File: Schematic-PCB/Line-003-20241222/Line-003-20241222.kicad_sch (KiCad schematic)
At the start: 233 parts, among them J1 Conn_MD, J2 VIN, SW1 RESET, U47 LM393, U48 LM393, U49 LM393, U50 LM393, U51 LM393, U52 LM393, U53 LM393, U54 LM393, U55 LM393, U56 LM393, U57 LM393, U58 LM393, U59 LM393, U60 LM393, U61 LM393, U62 LM393, U63 LM393, U64 LM393, U65 ATmega2560 Pro Board

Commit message: update: ラインセンサ基板 ver.003 を更新した
回路図のDRをした
いろいろ問題点ありそうだから、明日もう一回DRし直してからPCBいこか
出来れば明日、無理なら明後日ぐらいまでに必ず完成させよう！！
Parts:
- removed C14, C15, C16: 0.1uF, symbol Device:C_Small
- removed U60, U61, U62: LM393, symbol Comparator:LM393
- added JP10, JP7, JP8, JP9: Jumper_2_Small_Open, Jumper:SolderJumper-2_P1.3mm_Open_Pad1.0x1.5mm, symbol Jumper:Jumper_2_Small_Open
- added R86, R87: 100, Resistor_SMD:R_0603_1608Metric, symbol Device:R_Small
- C1, C10, C11, C12, C13, C17, C18, C2, C3, C4, C5, C6, C7, C8, C9: value 0.1uF -> 100nF; footprint (none) -> Capacitor_SMD:C_0603_1608Metric
- C21: renamed from C20; value C_Small -> 100nF; footprint (none) -> Capacitor_SMD:C_0603_1608Metric
- C23: footprint Capacitor_SMD:C_0603_1608Metric -> (none)
- R27, R28, R29, R30: value Line-PDWN -> Line-PDWN2
- U47, U48, U49, U50, U51, U52, U53, U54, U55, U56, U57, U58, U59, U63, U64: footprint (none) -> Package_SO:SOIC-8_3.9x4.9mm_P1.27mm
- renumbered C21 to C20, J2 to J1, J1 to J2, R78 to R77, R79 to R78, R80 to R79, R81 to R80, R82 to R81, R83 to R82, R84 to R83, R85 to R84, R86 to R85, R87 to R88
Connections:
- net 01: no longer U49.1, U50.1, U51.1, U52.1, U53.1, U54.1, U55.1, U56.1, U57.1, U58.1, U59.1
- net 02: no longer U49.7, U50.7, U51.7, U52.7, U53.7, U54.7, U55.7, U56.7, U57.7, U58.7, U59.7
- net 05: now also U49.1
- net 06: now also U49.7
- net 07: now also U50.1
- net 08: now also U50.7
- net 09: now also U51.1
- net 10: now also U51.7
- net 11: now also U52.1
- net 12: now also U52.7
- net 13: now also U53.1
- net 14: now also U53.7, U65.D22; no longer U65.D18
- net 15: now also U54.1, U65.D23; no longer U65.D19
- net 16: now also U54.7
- net 17: now also U55.1
- net 18: now also U55.7
- net 19: now also U56.1
- net 20: now also U56.7
- net 21: now also U57.1
- net 22: now also U57.7
- net 23: now also U58.1
- net 24: now also U58.7
- net 25: now also U59.1
- net 26: now also U59.7
- net Line01: no longer U49.3 (+), U50.3 (+), U51.3 (+), U52.3 (+), U53.3 (+), U54.3 (+), U55.3 (+), U56.3 (+), U57.3 (+), U58.3 (+), U59.3 (+)
- net Line02: no longer U49.5 (+), U50.5 (+), U51.5 (+), U52.5 (+), U53.5 (+), U54.5 (+), U55.5 (+), U56.5 (+), U57.5 (+), U58.5 (+), U59.5 (+)
- net Line05: now also U49.3 (+)
- net Line06: now also U49.5 (+)
- net Line07: now also U50.3 (+)
- net Line08: now also U50.5 (+)
- net Line09: now also U51.3 (+)
- net Line10: now also U51.5 (+)
- net Line11: now also U52.3 (+)
- net Line12: now also U52.5 (+)
- net Line13: now also U53.3 (+)
- net Line14: now also U53.5 (+)
- net Line15: now also U54.3 (+)
- net Line16: now also U54.5 (+)
- net Line17: now also U55.3 (+)
- net Line18: now also U55.5 (+)
- net Line19: now also U56.3 (+)
- net Line20: now also U56.5 (+)
- net Line21: now also U57.3 (+)
- net Line22: now also U57.5 (+)
- net Line23: now also U58.3 (+)
- net Line24: now also U58.5 (+)
- net Line25: now also U59.3 (+)
- net Line26: now also U59.5 (+)
- net RX: now also U65.D19, JP7.2 (B), JP9.2 (B); no longer J2.3 (Pin_3), U65.D21
- net SCL: now also U65.D21; no longer U65.D23
- net SDA: now also U65.D20; no longer U65.D22
- net TX: now also U65.D18, JP10.2 (B), JP8.2 (B); no longer J2.4 (Pin_4), U65.D20
- net MISO: no longer names the net of U65.MISO
- net MOSI: no longer names the net of U65.MOSI
- net SCK: no longer names the net of U65.SCK
- new net: JP10.1 (A), R87.2
- new net: J2.3 (Pin_3), JP7.1 (A), R86.1
- new net: JP9.1 (A), R86.2
- new net: J2.4 (Pin_4), JP8.1 (A), R87.1
- no-connect marks 21 -> 24
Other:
- moved on the sheet: C17, C18, J2, U63A, U63B, U63C, U64A, U64B, U64C

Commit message: add: ラインセンサ基板 ver.003を更新した
あと3Dプリンタ印刷用ファイルも追加した
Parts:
- C20: renamed from C23; footprint (none) -> Capacitor_THT:CP_Radial_D10.0mm_P5.00mm
- J1: footprint Connector_JST:JST_VH_B2P-VH-B_1x02_P3.96mm_Vertical -> Connector_JST:JST_XH_B2B-XH-A_1x02_P2.50mm_Vertical
- J2: footprint (none) -> @2024TOINIOT2-Line:Connector-MD
- renumbered C17 to C14, C18 to C15, C19 to C16, C20 to C17, C21 to C18, C22 to C19, C24 to C21, C25 to C22, U63 to U60, U64 to U61, U65 to U62
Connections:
- net 02: now also U48.1; no longer U47.7
- net 03: now also U48.7; no longer U48.1
- net 04: now also U49.1; no longer U48.7
- net 05: now also U49.7; no longer U49.1
- net 06: now also U50.1; no longer U49.7
- net 07: now also U50.7; no longer U50.1
- net 08: now also U51.7; no longer U50.7
- net 09: now also U52.1; no longer U51.1
- net 10: now also U52.7; no longer U51.7
- net 11: now also U53.1; no longer U52.1
- net 12: now also U53.7; no longer U52.7
- net 13: now also U54.1; no longer U53.1
- net 14: now also U54.7; no longer U53.7
- net 15: now also U55.7; no longer U54.1
- net 16: now also U56.1; no longer U54.7
- net 17: now also U56.7; no longer U55.1
- net 18: now also U57.1; no longer U55.7
- net 19: now also U57.7; no longer U56.1
- net 20: now also U58.7; no longer U56.7
- net 21: now also U59.1; no longer U57.1
- net 22: now also U59.7; no longer U57.7
- net 23: now also U60.1; no longer U58.1
- net 24: now also U60.7; no longer U58.7
- net 25: now also U61.1; no longer U59.1
- net 26: now also U61.7; no longer U59.7
- net B: now also U55.1; no longer U61.7
- net F: now also U47.7; no longer U60.1
- net L: now also U51.1; no longer U60.7
- net Line-B: now also U55.3 (+); no longer U61.5 (+)
- net Line-F: now also U47.5 (+); no longer U60.3 (+)
- net Line-L: now also U51.3 (+); no longer U60.5 (+)
- net Line-R: now also U58.3 (+); no longer U61.3 (+)
- net Line02: now also U48.3 (+); no longer U47.5 (+)
- net Line03: now also U48.5 (+); no longer U48.3 (+)
- net Line04: now also U49.3 (+); no longer U48.5 (+)
- net Line05: now also U49.5 (+); no longer U49.3 (+)
- net Line06: now also U50.3 (+); no longer U49.5 (+)
- net Line07: now also U50.5 (+); no longer U50.3 (+)
- net Line08: now also U51.5 (+); no longer U50.5 (+)
- net Line09: now also U52.3 (+); no longer U51.3 (+)
- net Line10: now also U52.5 (+); no longer U51.5 (+)
- net Line11: now also U53.3 (+); no longer U52.3 (+)
- net Line12: now also U53.5 (+); no longer U52.5 (+)
- net Line13: now also U54.3 (+); no longer U53.3 (+)
- net Line14: now also U54.5 (+); no longer U53.5 (+)
- net Line15: now also U55.5 (+); no longer U54.3 (+)
- net Line16: now also U56.3 (+); no longer U54.5 (+)
- net Line17: now also U56.5 (+); no longer U55.3 (+)
- net Line18: now also U57.3 (+); no longer U55.5 (+)
- net Line19: now also U57.5 (+); no longer U56.3 (+)
- net Line20: now also U58.5 (+); no longer U56.5 (+)
- net Line21: now also U59.3 (+); no longer U57.3 (+)
- net Line22: now also U59.5 (+); no longer U57.5 (+)
- net Line23: now also U60.3 (+); no longer U58.3 (+)
- net Line24: now also U60.5 (+); no longer U58.5 (+)
- net Line25: now also U61.3 (+); no longer U59.3 (+)
- net Line26: now also U61.5 (+); no longer U59.5 (+)
- net R: now also U58.1; no longer U61.1
- net Th: now also U60.2 (-), U60.6 (-), U61.2 (-), U61.6 (-); no longer U47.6 (-), U51.2 (-), U55.2 (-), U58.2 (-)
- net Th2: now also U47.6 (-), U51.2 (-), U55.2 (-), U58.2 (-); no longer U60.2 (-), U60.6 (-), U61.2 (-), U61.6 (-)

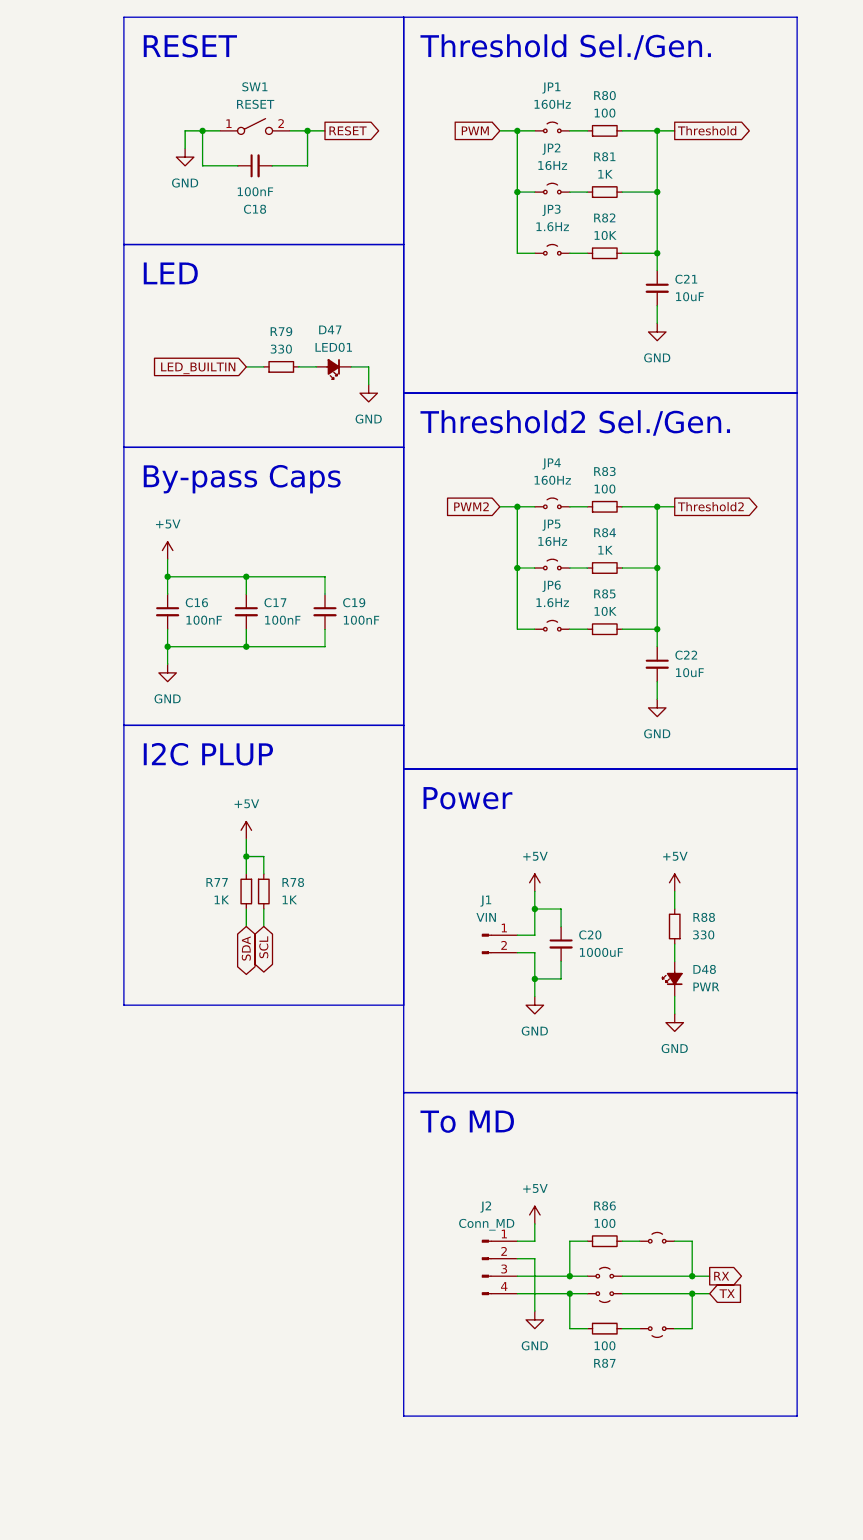
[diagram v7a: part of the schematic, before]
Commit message: update: ラインセンサ基板の回路とPCBを更新した
閾値用PWMの周波数選択用のジャンパの削除
基板外形の更新
など
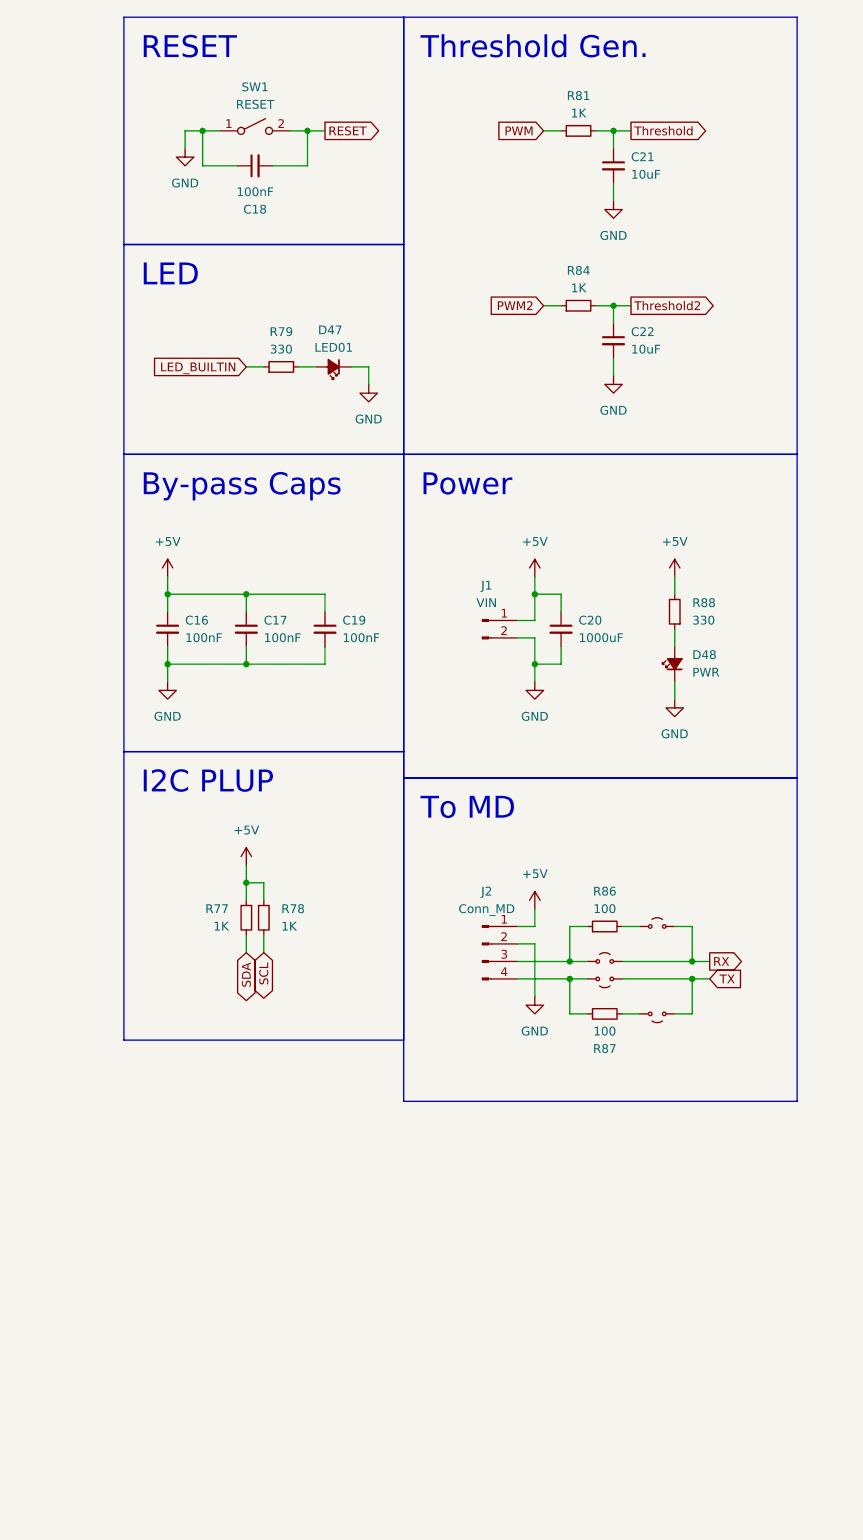
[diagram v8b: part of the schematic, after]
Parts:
- removed JP1, JP4: 160Hz, Jumper:SolderJumper-2_P1.3mm_Open_Pad1.0x1.5mm, symbol Jumper:Jumper_2_Small_Open
- removed JP2, JP5: 16Hz, Jumper:SolderJumper-2_P1.3mm_Open_Pad1.0x1.5mm, symbol Jumper:Jumper_2_Small_Open
- removed JP3, JP6: 1.6Hz, Jumper:SolderJumper-2_P1.3mm_Open_Pad1.0x1.5mm, symbol Jumper:Jumper_2_Small_Open
- removed R80, R83: 100, Resistor_SMD:R_0603_1608Metric, symbol Device:R_Small
- removed R82, R85: 10K, Resistor_SMD:R_0603_1608Metric, symbol Device:R_Small
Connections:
- net PWM: now also R81.1
- net PWM2: now also R84.1
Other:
- moved on the sheet: C16, C17, C19, C20, C21, C22, D48, J1, J2, R77, R78, R81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
